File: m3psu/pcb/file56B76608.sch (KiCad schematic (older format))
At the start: 48 parts

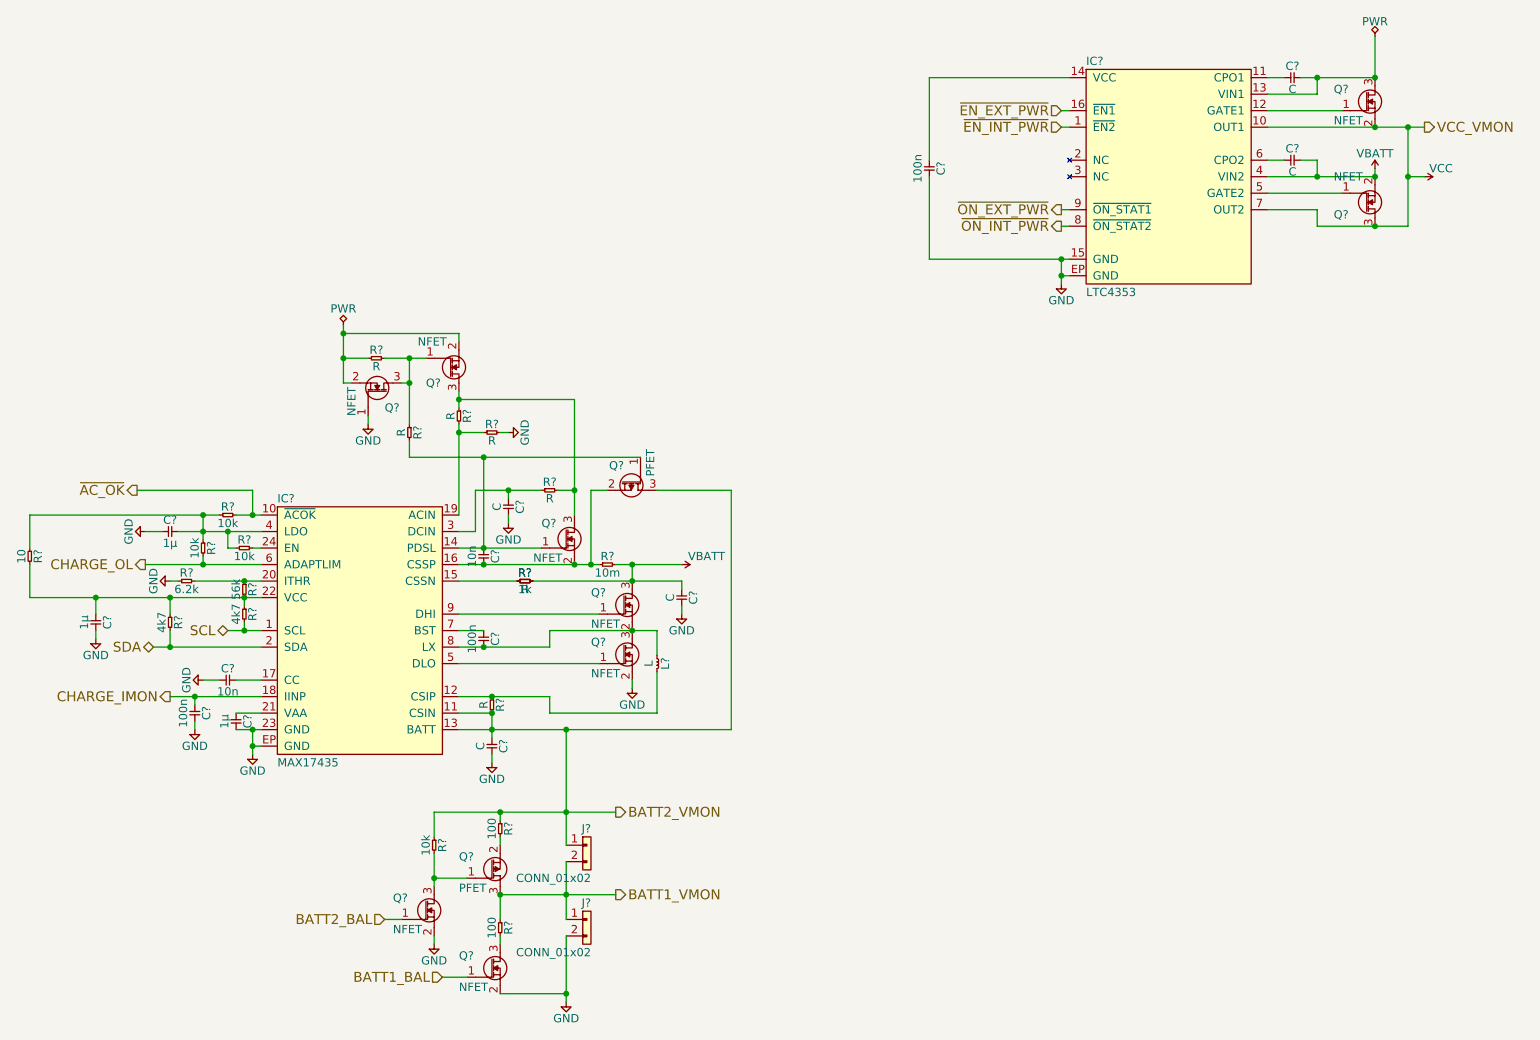
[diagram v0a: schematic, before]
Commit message: Finished passives for Li-ion Charger. Tweaked and cleaned up values in DC/DC Converter.
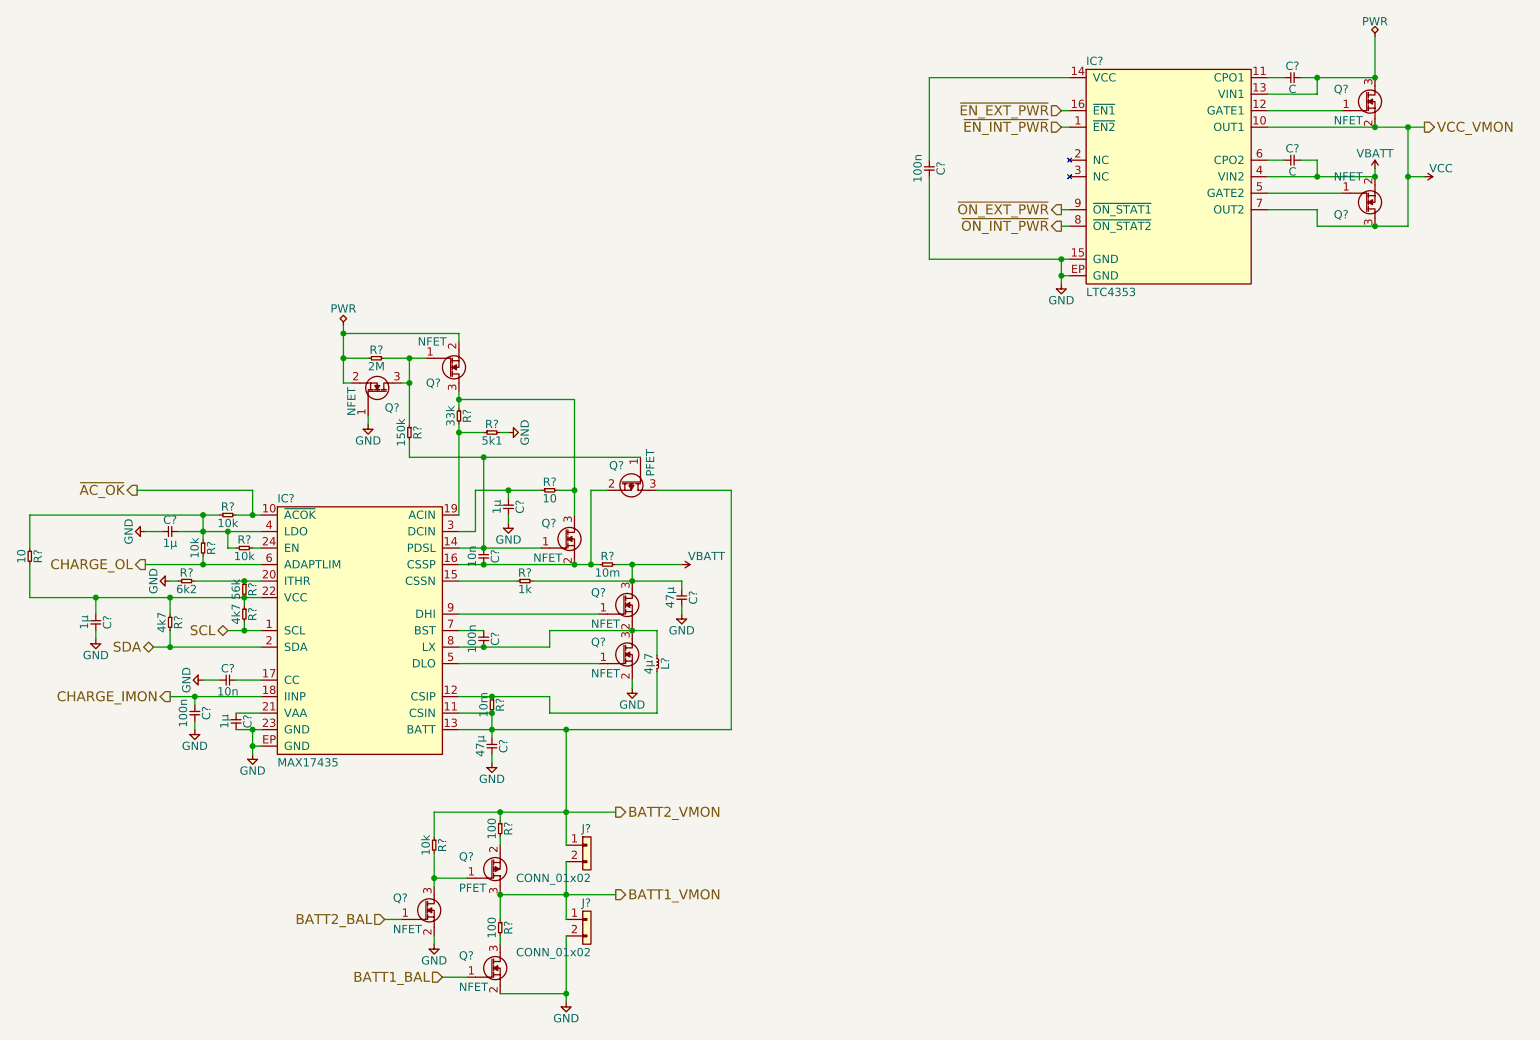
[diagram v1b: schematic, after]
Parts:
- removed R?: 1k, symbol R
- added R?: 1k, symbol R
- C? (x2): value C -> 47µ; Farnell (none) -> 1735538
- C?: value C -> 1µ
- L?: value L -> 4µ7; Farnell (none) -> 2309887
- R?: value R -> 10
- R?: value 6.2k -> 6k2
- R?: value R -> 10m
- R?: value R -> 2M
- R?: value R -> 150k
- R?: value R -> 33k
- R?: value R -> 5k1
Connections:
- net VBATT: now also R?.2
- net at IC?.15 (CSSN): now also R?.1
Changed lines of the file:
@@
 P 4700 3950
 F 0 "R?" H 4750 4000 50  0000 C CNN
-F 1 "R" H 4750 3900 50  0000 C CNN
+F 1 "10" H 4750 3900 50  0000 C CNN
 F 2 "" H 4700 3950 50  0001 C CNN
 F 3 "" H 4700 3950 50  0001 C CNN
@@
 F 3 "" H 2850 4300 50  0001 C CNN
 	1    2850 4300
-	1    0    0    -1
-$EndComp
-$Comp
-L R R?
-U 1 1 56B956BC
-P 4550 4500
-F 0 "R?" H 4600 4550 50  0000 C CNN
-F 1 "R" H 4600 4450 50  0000 C CNN
-F 2 "" H 4550 4500 50  0001 C CNN
-F 3 "" H 4550 4500 50  0001 C CNN
-	1    4550 4500
 	1    0    0    -1
 $EndComp
@@
 P 2500 4500
 F 0 "R?" H 2550 4550 50  0000 C CNN
-F 1 "6.2k" H 2550 4450 50  0000 C CNN
+F 1 "6k2" H 2550 4450 50  0000 C CNN
 F 2 "" H 2500 4500 50  0001 C CNN
 F 3 "" H 2500 4500 50  0001 C CNN
@@
 P 4400 5200
 F 0 "R?" H 4450 5250 50  0000 C CNN
-F 1 "R" H 4450 5150 50  0000 C CNN
+F 1 "10m" H 4450 5150 50  0000 C CNN
 F 2 "" H 4400 5200 50  0001 C CNN
 F 3 "" H 4400 5200 50  0001 C CNN
@@
 P 4400 5450
 F 0 "C?" H 4450 5520 50  0000 C CNN
-F 1 "C" H 4450 5380 50  0000 C CNN
+F 1 "47µ" H 4450 5380 50  0000 C CNN
 F 2 "" H 4400 5450 50  0001 C CNN
 F 3 "" H 4400 5450 50  0001 C CNN
+F 4 "1735538" H 4400 5450 60  0001 C CNN "Farnell"
 	1    4400 5450
 	0    1    1    0
@@
 P 5400 4950
 F 0 "L?" H 5450 5000 50  0000 C CNN
-F 1 "L" H 5450 4900 50  0000 C CNN
+F 1 "4µ7" H 5450 4900 50  0000 C CNN
 F 2 "" H 5400 4950 50  0001 C CNN
 F 3 "" H 5400 4950 50  0001 C CNN
+F 4 "2309887" H 5400 4950 60  0001 C CNN "Farnell"
 	1    5400 4950
 	0    1    1    0
@@
 P 5550 4550
 F 0 "C?" H 5600 4620 50  0000 C CNN
-F 1 "C" H 5600 4480 50  0000 C CNN
+F 1 "47µ" H 5600 4480 50  0000 C CNN
 F 2 "" H 5550 4550 50  0001 C CNN
 F 3 "" H 5550 4550 50  0001 C CNN
+F 4 "1735538" H 5550 4550 60  0001 C CNN "Farnell"
 	1    5550 4550
 	0    1    1    0
@@
 P 3650 3150
 F 0 "R?" H 3700 3200 50  0000 C CNN
-F 1 "R" H 3700 3100 50  0000 C CNN
+F 1 "2M" H 3700 3100 50  0000 C CNN
 F 2 "" H 3650 3150 50  0001 C CNN
 F 3 "" H 3650 3150 50  0001 C CNN
@@
 P 3900 3550
 F 0 "R?" H 3950 3600 50  0000 C CNN
-F 1 "R" H 3950 3500 50  0000 C CNN
+F 1 "150k" H 3950 3500 50  0000 C CNN
 F 2 "" H 3900 3550 50  0001 C CNN
 F 3 "" H 3900 3550 50  0001 C CNN
@@
 P 4500 4000
 F 0 "C?" H 4550 4070 50  0000 C CNN
-F 1 "C" H 4550 3930 50  0000 C CNN
+F 1 "1µ" H 4550 3930 50  0000 C CNN
 F 2 "" H 4500 4000 50  0001 C CNN
 F 3 "" H 4500 4000 50  0001 C CNN
@@
 P 4200 3450
 F 0 "R?" H 4250 3500 50  0000 C CNN
-F 1 "R" H 4250 3400 50  0000 C CNN
+F 1 "33k" H 4250 3400 50  0000 C CNN
 F 2 "" H 4200 3450 50  0001 C CNN
 F 3 "" H 4200 3450 50  0001 C CNN
@@
 P 4350 3600
 F 0 "R?" H 4400 3650 50  0000 C CNN
-F 1 "R" H 4400 3550 50  0000 C CNN
+F 1 "5k1" H 4400 3550 50  0000 C CNN
 F 2 "" H 4350 3600 50  0001 C CNN
 F 3 "" H 4350 3600 50  0001 C CNN
@@
 $EndComp
 Wire Wire Line
-	4900 3400 4900 3950
-Wire Wire Line
-	4900 3950 4900 4100
-Wire Wire Line
-	4200 3550 4200 3600
-Wire Wire Line
-	4200 3600 4200 4100
+	4900 3400 4900 4100
+Wire Wire Line
+	4200 3550 4200 4100
 Wire Wire Line
 	1600 4400 1600 4600
@@
 	4350 3750 4350 4300
 Wire Wire Line
-	3900 3750 4350 3750
-Wire Wire Line
-	4350 3750 5300 3750
+	3900 3750 5300 3750
 Connection ~ 3900 3300
 Wire Wire Line
@@
 	4200 3000 4200 3050
 Wire Wire Line
-	4200 3350 4200 3400
-Wire Wire Line
-	4200 3400 4200 3450
+	4200 3350 4200 3450
 Connection ~ 4200 3600
 Connection ~ 3900 3150
@@
 	4450 5950 4450 5900
 Wire Wire Line
-	4850 5400 4850 5900
-Wire Wire Line
-	4850 5900 4850 6100
+	4850 5400 4850 6100
 Wire Wire Line
 	4500 3950 4500 4000
@@
 	2850 5100 3000 5100
 Wire Wire Line
-	4300 3950 4500 3950
-Wire Wire Line
-	4500 3950 4700 3950
+	4300 3950 4700 3950
 Connection ~ 4500 3950
 Wire Wire Line
@@
 Connection ~ 4350 4300
 Wire Wire Line
-	4200 4300 4350 4300
-Wire Wire Line
-	4350 4300 4700 4300
+	4200 4300 4700 4300
 Connection ~ 4350 4400
 Wire Wire Line
 	3650 3500 3650 3550
 Wire Wire Line
-	3900 3150 3900 3300
-Wire Wire Line
-	3900 3300 3900 3550
-Wire Wire Line
-	3750 3150 3900 3150
-Wire Wire Line
-	3900 3150 4000 3150
+	3900 3150 3900 3550
+Wire Wire Line
+	3750 3150 4000 3150
 Connection ~ 3500 3150
 Wire Wire Line
@@
 	3500 3300 3550 3300
 Wire Wire Line
-	3500 2950 3500 3000
-Wire Wire Line
-	3500 3000 3500 3150
-Wire Wire Line
-	3500 3150 3500 3300
-Wire Wire Line
-	9950 2350 9750 2350
-Wire Wire Line
-	9750 2350 9400 2350
+	3500 2950 3500 3300
+Wire Wire Line
+	9950 2350 9400 2350
 Connection ~ 9950 1750
 Connection ~ 9950 2050
@@
 	9950 2050 10050 2050
 Wire Wire Line
-	9950 1750 9950 2050
-Wire Wire Line
-	9950 2050 9950 2350
-Wire Wire Line
-	9100 1750 9750 1750
-Wire Wire Line
-	9750 1750 9950 1750
-Wire Wire Line
-	9950 1750 10050 1750
+	9950 1750 9950 2350
+Wire Wire Line
+	9100 1750 10050 1750
 Connection ~ 9750 1750
 Connection ~ 9750 2350
@@
 	4050 5900 4050 6050
 Wire Wire Line
-	4050 6150 4050 6300
-Wire Wire Line
-	4050 6300 4050 6350
+	4050 6150 4050 6350
 Wire Wire Line
 	4050 6300 4250 6300
@@
 Connection ~ 4850 6400
 Wire Wire Line
-	4450 6400 4850 6400
-Wire Wire Line
-	4850 6400 5150 6400
+	4450 6400 5150 6400
 Connection ~ 4850 5900
 Wire Wire Line
-	4050 5900 4450 5900
-Wire Wire Line
-	4450 5900 4850 5900
-Wire Wire Line
-	4850 5900 5150 5900
-Wire Wire Line
-	4850 6650 4850 7000
-Wire Wire Line
-	4850 7000 4850 7050
-Wire Wire Line
-	4850 6200 4850 6400
-Wire Wire Line
-	4850 6400 4850 6550
+	4050 5900 5150 5900
+Wire Wire Line
+	4850 6650 4850 7050
+Wire Wire Line
+	4850 6200 4850 6550
 Connection ~ 5250 4400
 Wire Wire Line
 	5250 4400 5250 4500
 Wire Wire Line
-	5150 4400 5250 4400
-Wire Wire Line
-	5250 4400 5550 4400
-Wire Wire Line
-	4200 4400 4350 4400
-Wire Wire Line
-	4350 4400 4900 4400
-Wire Wire Line
-	4900 4400 5000 4400
-Wire Wire Line
-	5000 4400 5050 4400
+	5150 4400 5550 4400
+Wire Wire Line
+	4200 4400 5050 4400
 Connection ~ 5250 4500
 Wire Wire Line
@@
 	5550 4650 5550 4700
 Wire Wire Line
-	4650 4500 5250 4500
-Wire Wire Line
-	5250 4500 5550 4500
+	4650 4500 5550 4500
 Connection ~ 4400 5200
 Wire Wire Line
@@
 Connection ~ 5250 4800
 Wire Wire Line
-	4750 4800 5250 4800
-Wire Wire Line
-	5250 4800 5400 4800
+	4750 4800 5400 4800
 Wire Wire Line
 	4750 4900 4750 4800
@@
 Connection ~ 2800 4200
 Wire Wire Line
-	2800 4300 2800 4200
+	2800 4200 2800 4300
 Wire Wire Line
 	2950 4300 3000 4300
@@
 	7900 2650 7850 2650
 Wire Wire Line
-	7850 2550 7850 2650
-Wire Wire Line
-	7850 2650 7850 2700
-Wire Wire Line
-	7050 2550 7850 2550
-Wire Wire Line
-	7850 2550 7900 2550
+	7850 2550 7850 2700
+Wire Wire Line
+	7050 2550 7900 2550
 Wire Wire Line
 	7900 2350 7850 2350
@@
 	7900 1650 7850 1650
 Wire Wire Line
-	9100 2050 9400 2050
-Wire Wire Line
-	9400 2050 9750 2050
+	9100 2050 9750 2050
 Wire Wire Line
 	9100 1950 9200 1950
@@
 	9100 1450 9200 1450
 Wire Wire Line
-	4200 4900 4350 4900
-Wire Wire Line
-	4350 4900 4750 4900
+	4200 4900 4750 4900
 Wire Wire Line
 	4200 4800 4350 4800
@@
 	4200 5300 4400 5300
 Wire Wire Line
-	4200 5200 4400 5200
-Wire Wire Line
-	4400 5200 4750 5200
+	4200 5200 4750 5200
 Wire Wire Line
 	4400 5550 4400 5600
 Connection ~ 4400 5400
 Wire Wire Line
-	4400 5300 4400 5400
-Wire Wire Line
-	4400 5400 4400 5450
-Wire Wire Line
-	4200 5400 4400 5400
-Wire Wire Line
-	4400 5400 4850 5400
-Wire Wire Line
-	4850 5400 5850 5400
-Wire Wire Line
-	2600 4500 2900 4500
-Wire Wire Line
-	2900 4500 3000 4500
-Wire Wire Line
-	1600 4600 2000 4600
-Wire Wire Line
-	2000 4600 2450 4600
-Wire Wire Line
-	2450 4600 2900 4600
-Wire Wire Line
-	2900 4600 3000 4600
+	4400 5300 4400 5450
+Wire Wire Line
+	4200 5400 5850 5400
+Wire Wire Line
+	2600 4500 3000 4500
+Wire Wire Line
+	1600 4600 3000 4600
 Wire Wire Line
 	2000 4800 2000 4850
@@
 	2600 5250 2600 5200
 Wire Wire Line
-	2450 5200 2600 5200
-Wire Wire Line
-	2600 5200 3000 5200
+	2450 5200 3000 5200
 Connection ~ 2950 5500
 Connection ~ 2950 5400
 Wire Wire Line
-	2950 5400 2950 5500
-Wire Wire Line
-	2950 5500 2950 5550
+	2950 5400 2950 5550
 Wire Wire Line
 	3000 5500 2950 5500
 Wire Wire Line
-	2850 5400 2950 5400
-Wire Wire Line
-	2950 5400 3000 5400
+	2850 5400 3000 5400
 Wire Wire Line
 	3000 5300 2850 5300
@@
 	2650 4400 2650 4350
 Wire Wire Line
-	2650 4100 2650 4200
-Wire Wire Line
-	2650 4200 2650 4250
-Wire Wire Line
-	1600 4100 2650 4100
-Wire Wire Line
-	2650 4100 2750 4100
-Wire Wire Line
-	2850 4100 2950 4100
-Wire Wire Line
-	2950 4100 3000 4100
+	2650 4100 2650 4250
+Wire Wire Line
+	1600 4100 2750 4100
+Wire Wire Line
+	2850 4100 3000 4100
 Connection ~ 2650 4200
 Connection ~ 2650 4400
 Wire Wire Line
-	2300 4400 2650 4400
-Wire Wire Line
-	2650 4400 3000 4400
-Wire Wire Line
-	2500 4200 2650 4200
-Wire Wire Line
-	2650 4200 2800 4200
-Wire Wire Line
-	2800 4200 3000 4200
+	2300 4400 3000 4400
+Wire Wire Line
+	2500 4200 3000 4200
 Connection ~ 2900 4500
 Wire Wire Line
@@
 	2900 4600 2900 4650
 Wire Wire Line
-	2350 4900 2450 4900
-Wire Wire Line
-	2450 4900 3000 4900
-Wire Wire Line
-	2800 4800 2900 4800
-Wire Wire Line
-	2900 4800 3000 4800
+	2350 4900 3000 4900
+Wire Wire Line
+	2800 4800 3000 4800
 Wire Wire Line
 	3900 3650 3900 3750
@@
 	9400 1550 9400 1450
 Wire Wire Line
-	9300 1450 9400 1450
-Wire Wire Line
-	9400 1450 9750 1450
+	9300 1450 9750 1450
 Connection ~ 9400 1450
 Connection ~ 9750 1450
